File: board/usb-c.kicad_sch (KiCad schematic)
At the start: 4 parts, among them J1 USB4105-GF-A

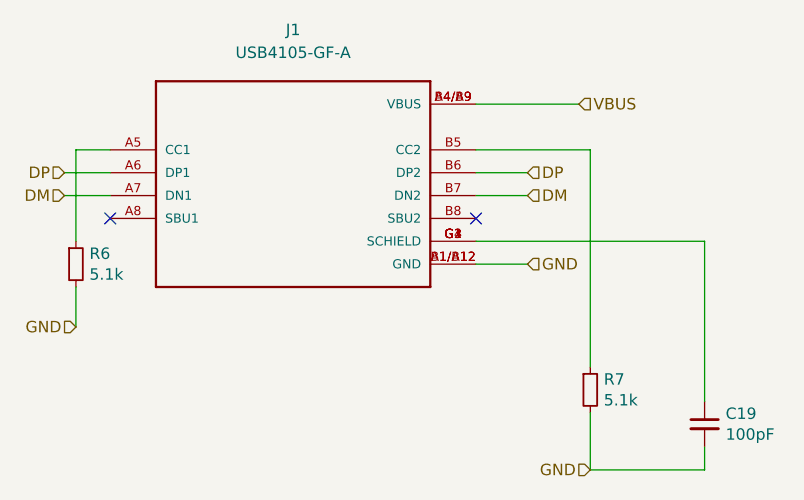
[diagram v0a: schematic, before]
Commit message: added straping support for different interfaces
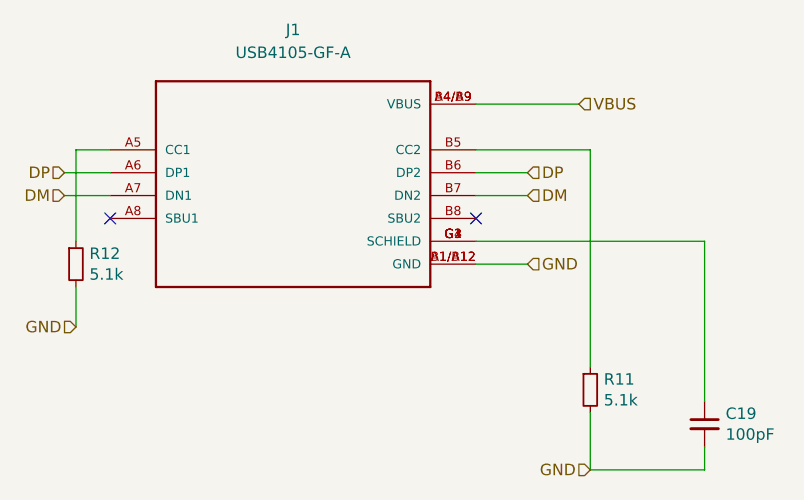
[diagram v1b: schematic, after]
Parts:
- renumbered R7 to R11, R6 to R12
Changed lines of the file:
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@@
   (symbol (lib_id "Device:R_Small") (at 175.895 123.825 0) (unit 1)
     (in_bom yes) (on_board yes) (dnp no)
-    (property "Reference" "R7" (at 177.3936 122.6566 0)
+    (property "Reference" "R11" (at 177.3936 122.6566 0)
       (effects (font (size 1.27 1.27)) (justify left))
     )
@@
       (project "board"
         (path "/57732dd3-1162-4c3f-88bd-31bf473d124d/77ae33e1-4e6d-45bf-ad31-337c508fa70d"
-          (reference "R7") (unit 1)
+          (reference "R11") (unit 1)
         )
       )
@@
   (symbol (lib_id "Device:R_Small") (at 118.745 109.855 0) (unit 1)
     (in_bom yes) (on_board yes) (dnp no)
-    (property "Reference" "R6" (at 120.2436 108.6866 0)
+    (property "Reference" "R12" (at 120.2436 108.6866 0)
       (effects (font (size 1.27 1.27)) (justify left))
     )
@@
       (project "board"
         (path "/57732dd3-1162-4c3f-88bd-31bf473d124d/77ae33e1-4e6d-45bf-ad31-337c508fa70d"
-          (reference "R6") (unit 1)
+          (reference "R12") (unit 1)
         )
       )
